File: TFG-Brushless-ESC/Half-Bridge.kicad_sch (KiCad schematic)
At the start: 21 parts, among them Q1 TK58E06N1, Q7 TK58E06N1, U5 IR2101, U9 INA180A3

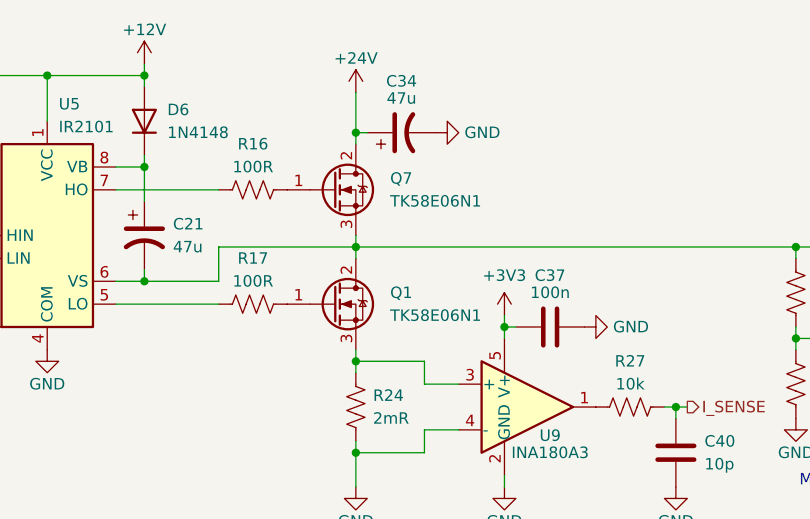
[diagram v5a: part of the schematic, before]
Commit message: Footprint corrections
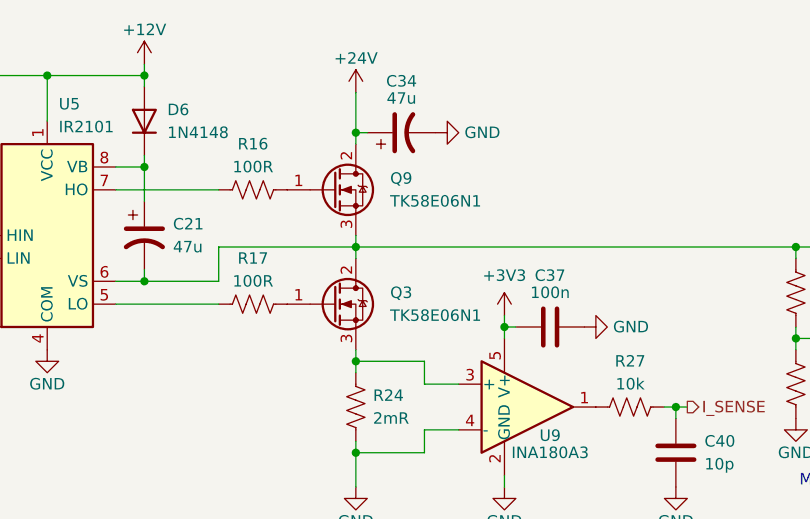
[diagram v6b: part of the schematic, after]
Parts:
- D9: footprint (none) -> Diode_SMD:D_0603_1608Metric
- R24: footprint (none) -> Resistor_SMD:R_2512_6332Metric
- renumbered Q1 to Q3, Q7 to Q9
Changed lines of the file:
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@@
 		(dnp no)
 		(fields_autoplaced yes)
-		(property "Reference" "Q7"
+		(property "Reference" "Q9"
 			(at 83.82 46.9899 0)
 			(effects
@@
 		(dnp no)
 		(fields_autoplaced yes)
-		(property "Reference" "Q1"
+		(property "Reference" "Q3"
 			(at 83.82 59.6899 0)
 			(effects
@@
 			)
 		)
-		(property "Footprint" ""
+		(property "Footprint" "Resistor_SMD:R_2512_6332Metric"
 			(at 81.026 72.644 90)
 			(effects
@@
 			)
 		)
-		(property "Footprint" ""
+		(property "Footprint" "Diode_SMD:D_0603_1608Metric"
 			(at 173.355 66.04 0)
 			(effects

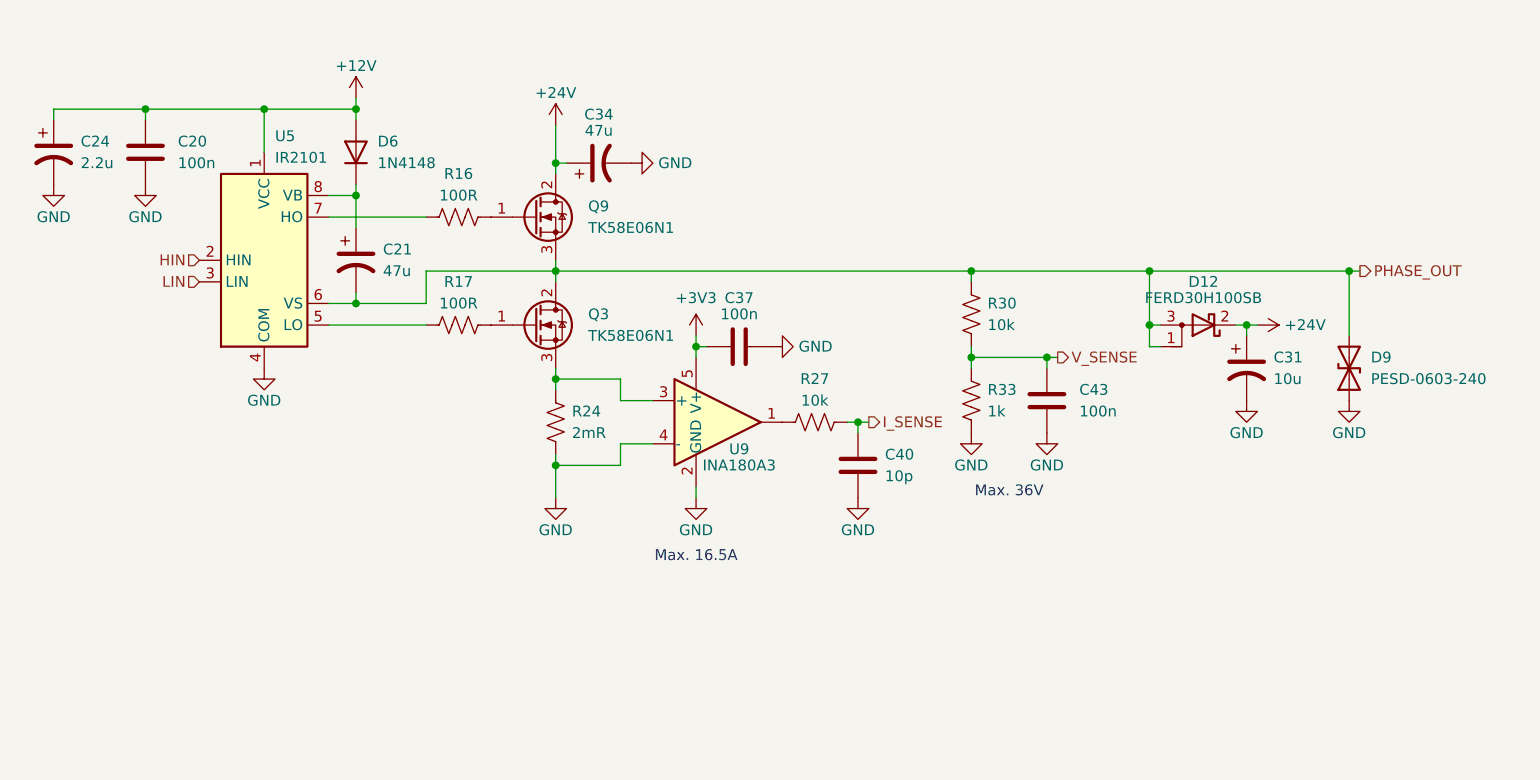
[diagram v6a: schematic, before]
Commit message: Half bridges done
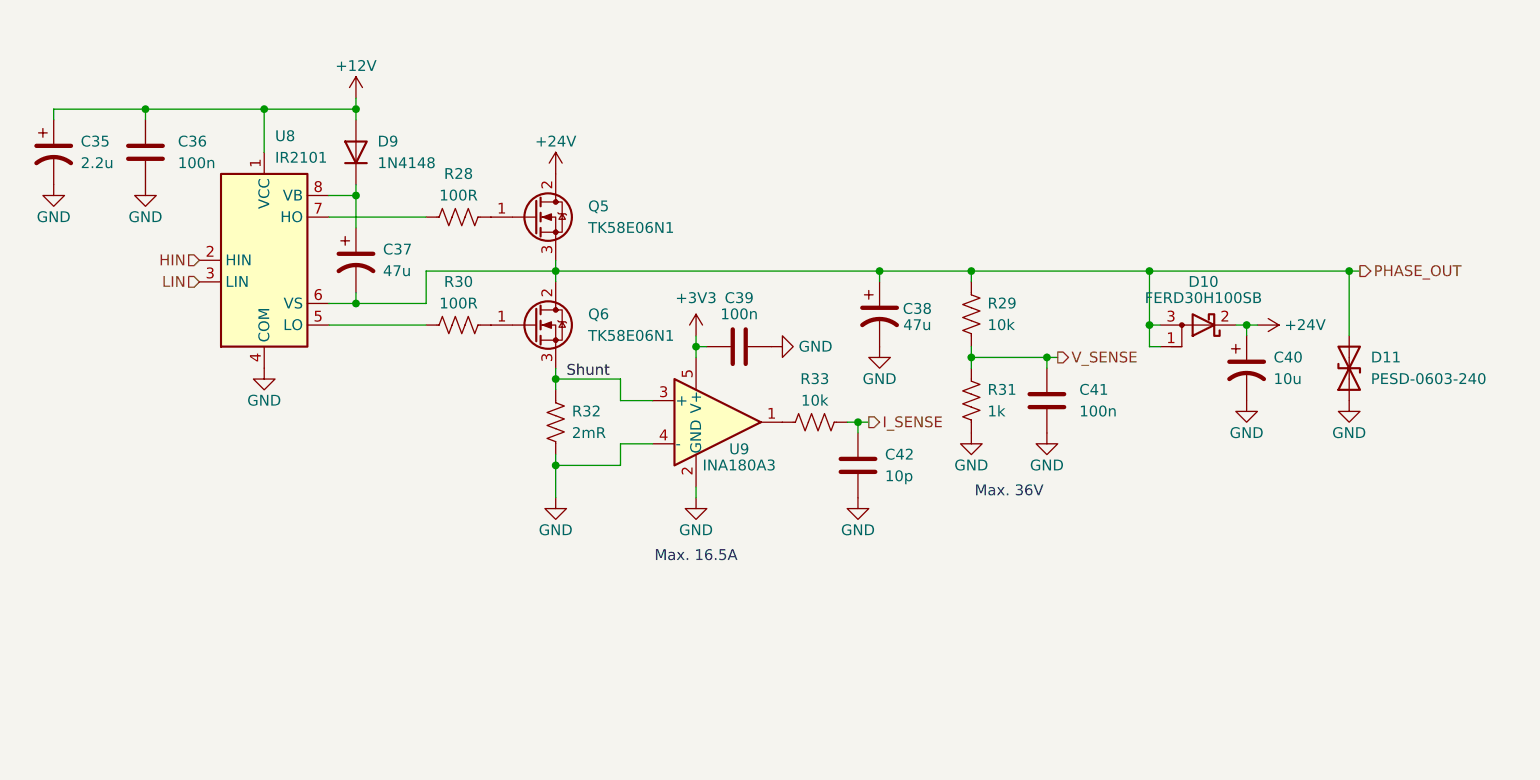
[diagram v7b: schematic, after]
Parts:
- renumbered C24 to C35, C20 to C36, C21 to C37, C34 to C38, C37 to C39, C31 to C40, C43 to C41, C40 to C42, D12 to D10, D9 to D11, D6 to D9, Q9 to Q5, Q3 to Q6, R16 to R28, R30 to R29, R17 to R30, R33 to R31, R24 to R32, R27 to R33, U5 to U8
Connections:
- net +24V: no longer C38.1
- net PHASE_OUT: now also C38.1
- net Shunt: now reaches Q6.3 (S), R32.1, U9.3 (+)
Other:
- moved on the sheet: C38

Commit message: temporary unifinished layout
tht components and initia layout
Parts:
- removed C40: 10u, Capacitor_THT:CP_Radial_D5.0mm_P2.00mm, symbol Device:C_Polarized_US
- removed D10: FERD30H100SB, Package_TO_SOT_SMD:TO-252-2, symbol Device:D_Schottky_AKA
- removed D11: PESD-0603-240, Diode_SMD:D_0603_1608Metric, symbol Device:D_TVS
- added D7: SMAJ16CA-13-F, Diode_SMD:D_SMA, symbol Device:D_TVS
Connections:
- net GND: now also D7.1 (A1)
- net PHASE_OUT: now also D7.2 (A2)
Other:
- moved on the sheet: C35, C36, C37, C38, C39, C41, C42, D9, Q5, Q6, R28, R29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
